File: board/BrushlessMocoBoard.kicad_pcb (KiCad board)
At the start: 4 copper layers, 107.6 x 86.6 mm, 117 parts, among them J1 Conn_01x03, J2 Conn_01x03, J3 Conn_01x03, SW1 SW_Push, SW2 SW_Push, U1 STSPIN32G4TR, U2 SN65HVD232

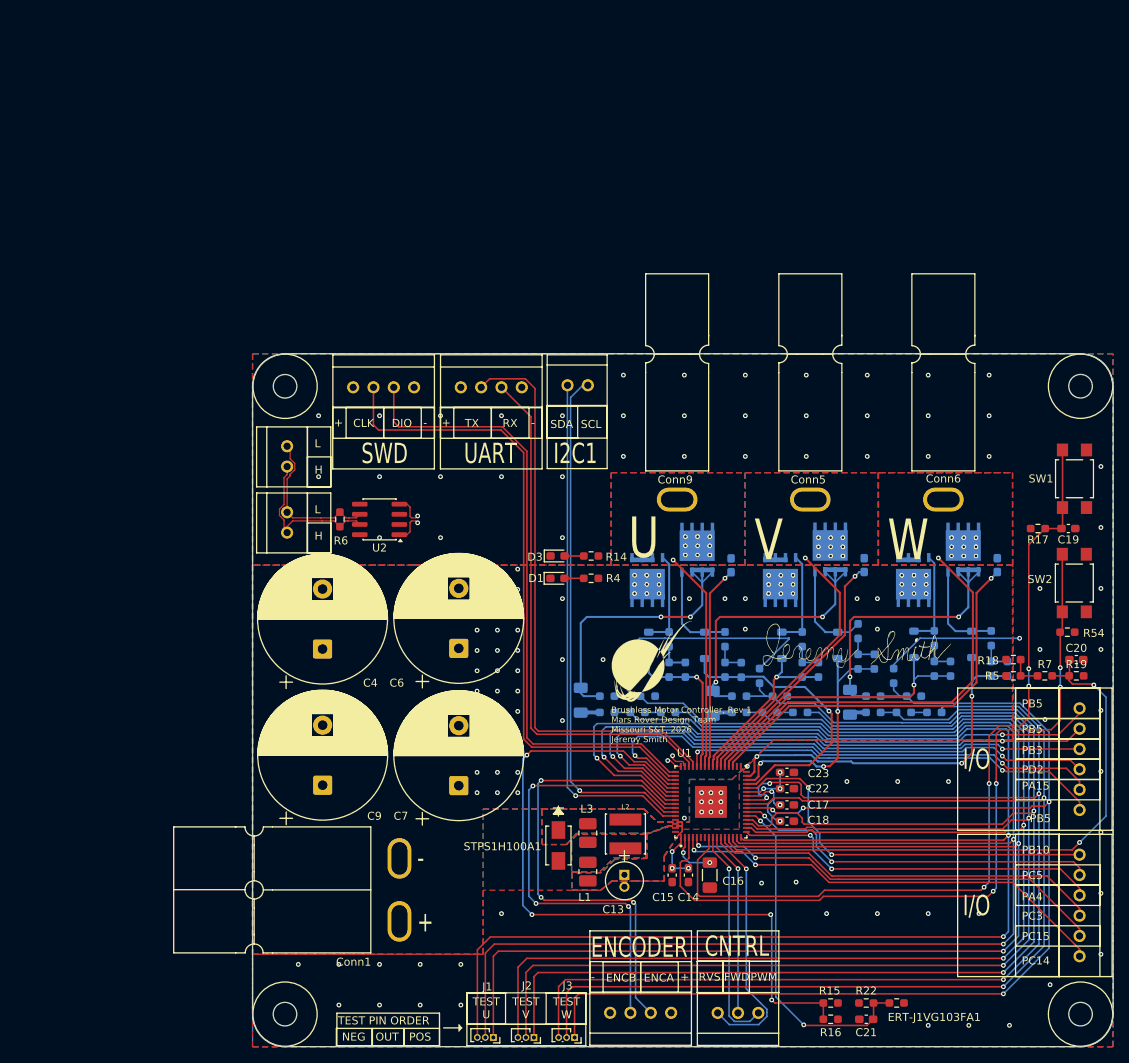
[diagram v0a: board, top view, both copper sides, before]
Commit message: Fixed many issues found in Rev1 review prior to order
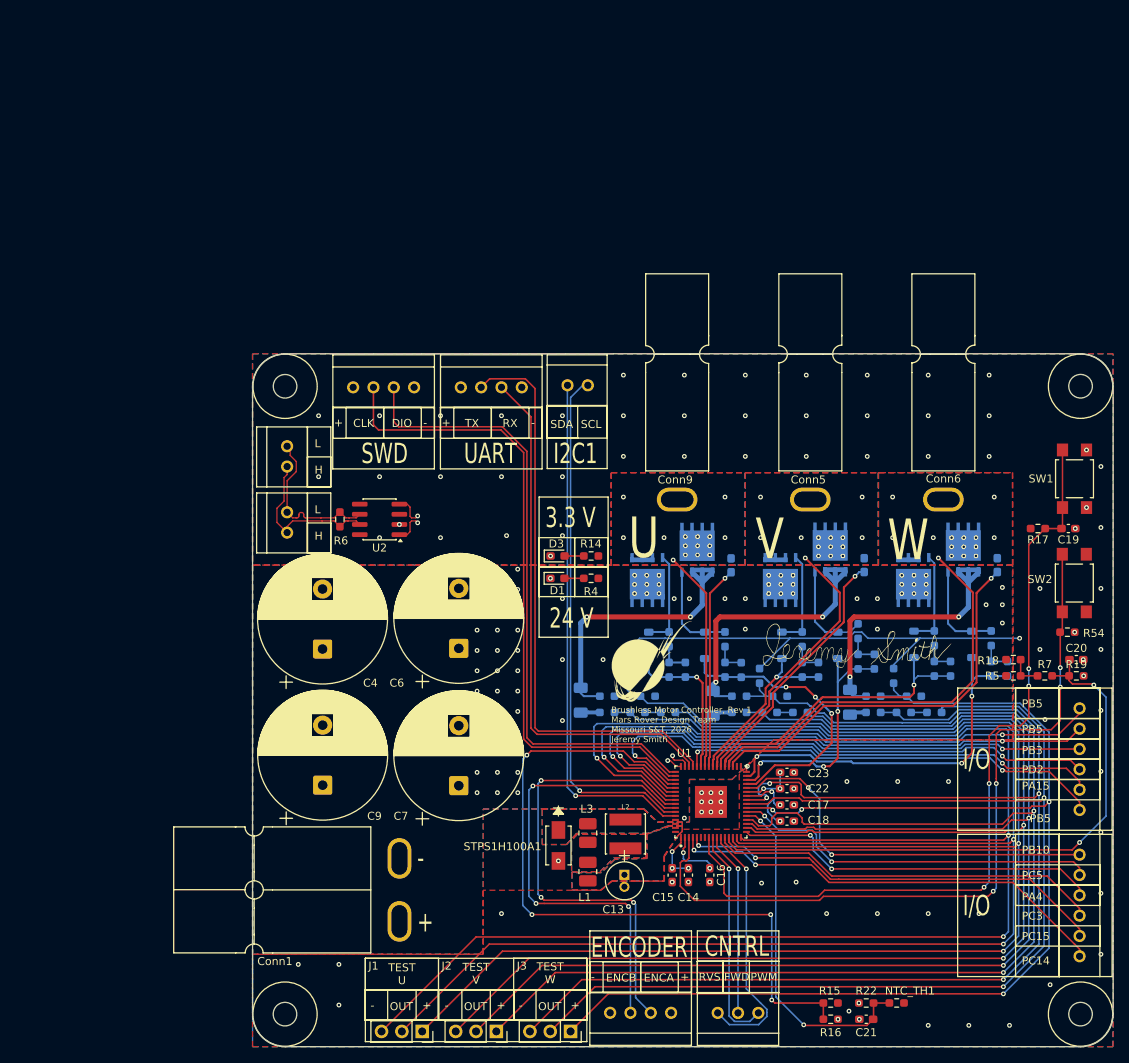
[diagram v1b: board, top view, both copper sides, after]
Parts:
- C13: value EEAGA1E100H -> 10 µF / 25 V
- C16: value 100 μF / 6.3 V -> 100 nF / 6.3 V; footprint Capacitor_SMD:C_1206_3216Metric_Pad1.33x1.80mm_HandSolder -> Capacitor_SMD:C_0603_1608Metric_Pad1.08x0.95mm_HandSolder
- J1, J2, J3: footprint Connector_PinSocket_1.00mm:PinSocket_1x03_P1.00mm_Vertical -> Connector_PinSocket_2.54mm:PinSocket_1x03_P2.54mm_Vertical
- R14: value 100 Ω -> 470 Ω
- R4: value 1.5 kΩ -> 6.8 kΩ
- moved J1 8.93 mm to (51.0, 125.2)
- moved J2 4.76 mm to (60.3, 125.2)
- moved J3 0.91 mm to (69.6, 125.2)
- renumbered ERT-J1VG103FA1 to NTC_TH1, MOSFET1 to Q1, MOSFET2 to Q2, MOSFET3 to Q3, MOSFET4 to Q4, MOSFET5 to Q5, MOSFET6 to Q6
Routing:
- net +3.3V: track 74.8 -> 92.7 mm, vias 81 -> 77
- net /Half-Bridges & Current Sensing/OPN_U: track 188.5 -> 193.8 mm
- net /Half-Bridges & Current Sensing/OPO_U: track 182.5 -> 186.4 mm
- net Net-(U1-PG10): track 105.6 -> 102.4 mm
- net /Half-Bridges & Current Sensing/OPP_W: track 157.4 -> 154.7 mm
- net /Half-Bridges & Current Sensing/OPP_U: track 194.4 -> 197.0 mm
- net /Half-Bridges & Current Sensing/OPN_V: track 171.6 -> 173.9 mm
- net /Half-Bridges & Current Sensing/OPO_W: track 147.0 -> 145.5 mm
- net /Half-Bridges & Current Sensing/OPO_V: track 164.7 -> 165.9 mm
- net CAN-: track 19.2 -> 20.2 mm
- net GND: track 1.54 -> 2.29 mm, vias 10 -> 30
- net /Half-Bridges & Current Sensing/GLS_U: vias 1 -> 3
- net /Half-Bridges & Current Sensing/OUT_W: vias 10 -> 15
- net /Half-Bridges & Current Sensing/OUT_V: vias 10 -> 15
- net 24 V: vias 76 -> 80
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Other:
- board text added: "24 V"
- board text added: "3.3 V"
- board text removed: "NEG"
- board text removed: "POS"
- board text removed: "TEST PIN ORDER"

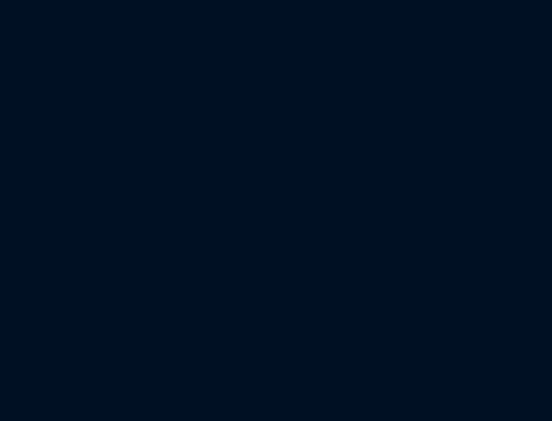
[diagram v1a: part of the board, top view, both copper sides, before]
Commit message: Added Cvm to schematic, need to add to layout as well
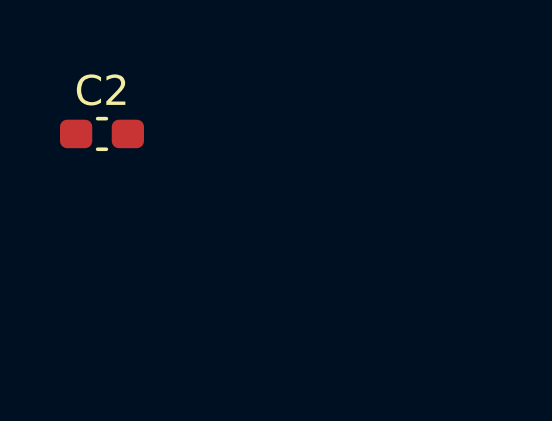
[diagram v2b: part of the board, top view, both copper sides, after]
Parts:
- added C2: 220 nF / 100 V, Capacitor_SMD:C_0603_1608Metric_Pad1.08x0.95mm_HandSolder, F.Cu at (1.68, 0.76)
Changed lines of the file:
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@@
+		)
+	)
+	(footprint "Capacitor_SMD:C_0603_1608Metric_Pad1.08x0.95mm_HandSolder"
+		(layer "F.Cu")
+		(at 1.675 0.755)
+		(descr "Capacitor SMD 0603 (1608 Metric), square (rectangular) end terminal, IPC-7351 nominal with elongated pad for handsoldering. (Body size source: IPC-SM-782 page 76, https://www.pcb-3d.com/wordpress/wp-content/uploads/ipc-sm-782a_amendment_1_and_2.pdf), generated with kicad-footprint-generator")
+		(tags "capacitor handsolder")
+		(property "Reference" "C2"
+			(at 0 -1.43 0)
+			(layer "F.SilkS")
+			(effects
+				(font
+					(size 1 1)
+					(thickness 0.15)
+				)
+			)
+		)
+		(property "Value" "220 nF / 100 V"
+			(at 0 1.43 0)
+			(layer "F.Fab")
+			(effects
+				(font
+					(size 1 1)
+					(thickness 0.15)
+				)
+			)
+		)
+		(property "Datasheet" "~"
+			(at 0 0 0)
+			(layer "F.Fab")
+			(hide yes)
+			(effects
+				(font
+					(size 1.27 1.27)
+					(thickness 0.15)
+				)
+			)
+		)
+		(property "Description" "Unpolarized capacitor"
+			(at 0 0 0)
+			(layer "F.Fab")
+			(hide yes)
+			(effects
+				(font
+					(size 1.27 1.27)
+					(thickness 0.15)
+				)
+			)
+		)
+		(property ki_fp_filters "C_*")
+		(sheetname "/MCU/")
+		(sheetfile "MCU.kicad_sch")
+		(attr smd)
+		(fp_line
+			(start -0.146267 -0.51)
+			(end 0.146267 -0.51)
+			(stroke
+				(width 0.12)
+				(type solid)
+			)
+			(layer "F.SilkS")
+		)
+		(fp_line
+			(start -0.146267 0.51)
+			(end 0.146267 0.51)
+			(stroke
+				(width 0.12)
+				(type solid)
+			)
+			(layer "F.SilkS")
+		)
+		(fp_line
+			(start -1.65 -0.73)
+			(end 1.65 -0.73)
+			(stroke
+				(width 0.05)
+				(type solid)
+			)
+			(layer "F.CrtYd")
+		)
+		(fp_line
+			(start -1.65 0.73)
+			(end -1.65 -0.73)
+			(stroke
+				(width 0.05)
+				(type solid)
+			)
+			(layer "F.CrtYd")
+		)
+		(fp_line
+			(start 1.65 -0.73)
+			(end 1.65 0.73)
+			(stroke
+				(width 0.05)
+				(type solid)
+			)
+			(layer "F.CrtYd")
+		)
+		(fp_line
+			(start 1.65 0.73)
+			(end -1.65 0.73)
+			(stroke
+				(width 0.05)
+				(type solid)
+			)
+			(layer "F.CrtYd")
+		)
+		(fp_line
+			(start -0.8 -0.4)
+			(end 0.8 -0.4)
+			(stroke
+				(width 0.1)
+				(type solid)
+			)
+			(layer "F.Fab")
+		)
+		(fp_line
+			(start -0.8 0.4)
+			(end -0.8 -0.4)
+			(stroke
+				(width 0.1)
+				(type solid)
+			)
+			(layer "F.Fab")
+		)
+		(fp_line
+			(start 0.8 -0.4)
+			(end 0.8 0.4)
+			(stroke
+				(width 0.1)
+				(type solid)
+			)
+			(layer "F.Fab")
+		)
+		(fp_line
+			(start 0.8 0.4)
+			(end -0.8 0.4)
+			(stroke
+				(width 0.1)
+				(type solid)
+			)
+			(layer "F.Fab")
+		)
+		(fp_text user "${REFERENCE}"
+			(at 0 0 0)
+			(layer "F.Fab")
+			(effects
+				(font
+					(size 0.4 0.4)
+					(thickness 0.06)
+				)
+			)
+		)
+		(pad "1" smd roundrect
+			(at -0.8625 0)
+			(size 1.075 0.95)
+			(layers "F.Cu" "F.Mask" "F.Paste")
+			(roundrect_rratio 0.25)
+			(net 4 "24 V")
+			(pintype "passive")
+		)
+		(pad "2" smd roundrect
+			(at 0.8625 0)
+			(size 1.075 0.95)
+			(layers "F.Cu" "F.Mask" "F.Paste")
+			(roundrect_rratio 0.25)
+			(net 77 "GND")
+			(pintype "passive")
+		)
+		(embedded_fonts no)
+		(model "${KICAD9_3DMODEL_DIR}/Capacitor_SMD.3dshapes/C_0603_1608Metric.step"
+			(offset
+				(xyz 0 0 0)
+			)
+			(scale
+				(xyz 1 1 1)
+			)
+			(rotate
+				(xyz 0 0 0)
+			)
 		)
 	)

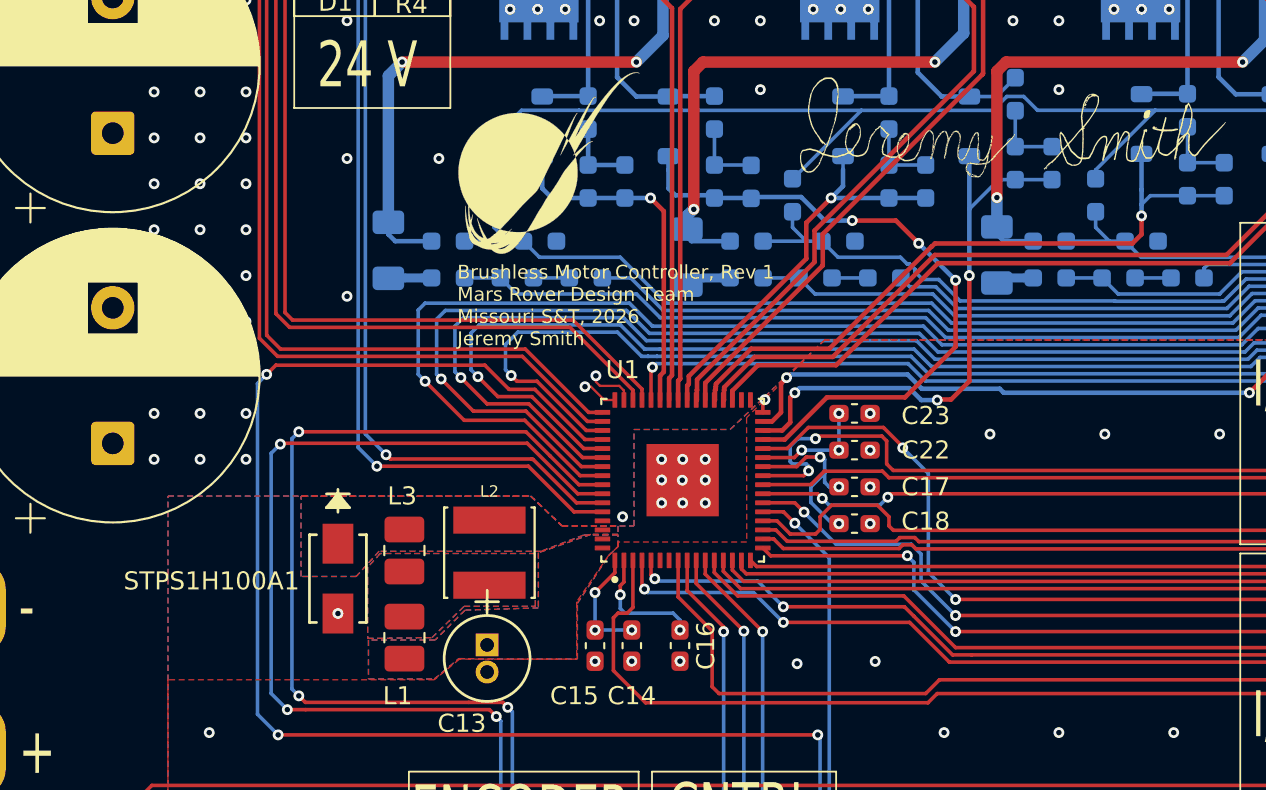
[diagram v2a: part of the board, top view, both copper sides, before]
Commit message: Added footprints to board library
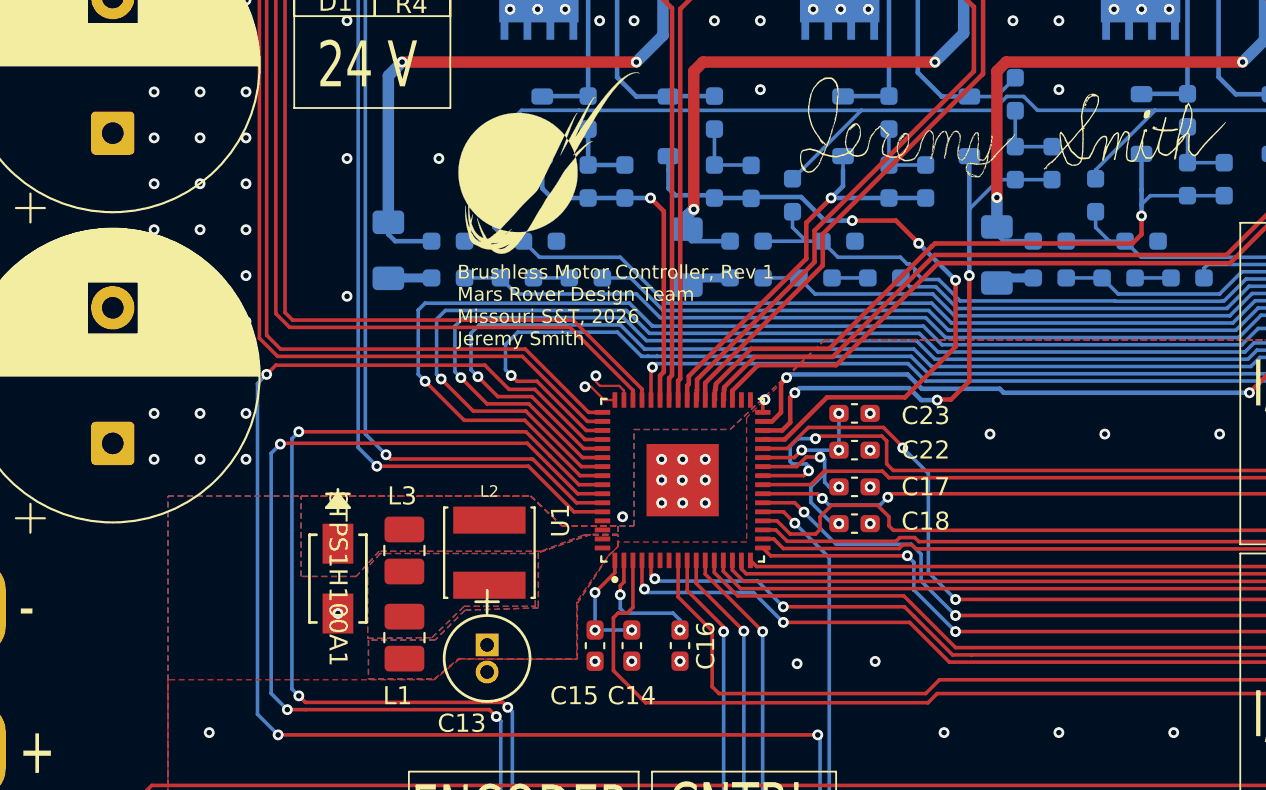
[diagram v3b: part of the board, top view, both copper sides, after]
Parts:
- Q1, Q2, Q3, Q4, Q5, Q6: footprint BoCoFootprintLibrary:PG-TDSON-8_INF -> BrushlessMocoBoard:PG-TDSON-8_INF
- STPS1H100A1: footprint BoCoFootprintLibrary:SMA_STM -> BrushlessMocoBoard:SMA_STM
- U1: footprint STSPIN32G4TR:QFN50P900X900X100-65N -> BrushlessMocoBoard:QFN50P900X900X100-65N
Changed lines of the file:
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@@
 		(embedded_fonts no)
 	)
-	(footprint "STSPIN32G4TR:QFN50P900X900X100-65N"
+	(footprint "BrushlessMocoBoard:QFN50P900X900X100-65N"
 		(layer "F.Cu")
 		(at 87.142 96.53 90)
 		(property "Reference" "U1"
-			(at 6.106 -3.322 180)
+			(at -2.235 -6.75 90)
 			(layer "F.SilkS")
 			(effects
@@
 		)
 		(property "Value" "STSPIN32G4TR"
-			(at 0 0 180)
+			(at 7.925 6.75 90)
 			(layer "F.Fab")
 			(effects
@@
 		)
 	)
-	(footprint "BoCoFootprintLibrary:SMA_STM"
+	(footprint "BrushlessMocoBoard:SMA_STM"
 		(layer "F.Cu")
 		(at 68.077242 101.973356 -90)
 		(tags "STPS1H100A ")
 		(property "Reference" "STPS1H100A1"
-			(at 0.134644 6.990242 0)
+			(at 0 0 270)
 			(unlocked yes)
 			(layer "F.SilkS")
@@
 		)
 		(property "Datasheet" "https://www.st.com/resource/en/datasheet/stps1h100.pdf"
-			(at 0 0 90)
+			(at 0 0 270)
 			(layer "F.Fab")
 			(hide yes)
@@
 		)
 		(property "Description" ""
-			(at 0 0 90)
+			(at 0 0 270)
 			(layer "F.Fab")
 			(hide yes)
@@
 			(pintype "unspecified")
 		)
+		(zone
+			(net 0)
+			(net_name "")
+			(layer "F.Cu")
+			(hatch full 0.508)
+			(connect_pads
+				(clearance 0)
+			)
+			(min_thickness 0.254)
+			(filled_areas_thickness no)
+			(keepout
+				(tracks not_allowed)
+				(vias not_allowed)
+				(pads allowed)
+				(copperpour not_allowed)
+				(footprints allowed)
+			)
+			(placement
+				(enabled no)
+				(sheetname "")
+			)
+			(fill
+				(thermal_gap 0.508)
+				(thermal_bridge_width 0.508)
+			)
+			(polygon
+				(pts
+					(xy 69.474242 101.198656) (xy 69.474242 102.748056) (xy 66.680242 102.748056) (xy 66.680242 101.198656)
+				)
+			)
+		)
 		(embedded_fonts no)
 	)
@@
 		)
 	)
-	(footprint "BoCoFootprintLibrary:PG-TDSON-8_INF"
+	(footprint "BrushlessMocoBoard:PG-TDSON-8_INF"
 		(layer "B.Cu")
 		(at 112.465201 68.797496 -90)
 		(tags "BSC035N10NS5ATMA1 ")
 		(property "Reference" "Q5"
-			(at -4.535496 0.324201 0)
+			(at 0 0 90)
 			(unlocked yes)
 			(layer "B.SilkS")
@@
 		)
 	)
-	(footprint "BoCoFootprintLibrary:PG-TDSON-8_INF"
+	(footprint "BrushlessMocoBoard:PG-TDSON-8_INF"
 		(layer "B.Cu")
 		(at 118.688201 64.987496 90)
 		(tags "BSC035N10NS5ATMA1 ")
 		(property "Reference" "Q6"
-			(at -4.735504 0.437799 0)
+			(at 0 0 270)
 			(unlocked yes)
 			(layer "B.SilkS")
@@
 		)
 	)
-	(footprint "BoCoFootprintLibrary:PG-TDSON-8_INF"
+	(footprint "BrushlessMocoBoard:PG-TDSON-8_INF"
 		(layer "B.Cu")
 		(at 95.828201 68.797496 -90)
 		(tags "BSC035N10NS5ATMA1 ")
 		(property "Reference" "Q3"
-			(at -4.535496 0.197201 0)
+			(at 0 0 90)
 			(unlocked yes)
 			(layer "B.SilkS")
@@
 		)
 	)
-	(footprint "BoCoFootprintLibrary:PG-TDSON-8_INF"
+	(footprint "BrushlessMocoBoard:PG-TDSON-8_INF"
 		(layer "B.Cu")
 		(at 85.4202 65.0113 90)
 		(tags "BSC035N10NS5ATMA1 ")
 		(property "Reference" "Q2"
-			(at -4.8387 0.0508 0)
+			(at 0 0 270)
 			(unlocked yes)
 			(layer "B.SilkS")
@@
 		)
 	)
-	(footprint "BoCoFootprintLibrary:PG-TDSON-8_INF"
+	(footprint "BrushlessMocoBoard:PG-TDSON-8_INF"
 		(layer "B.Cu")
 		(at 102.051201 64.974796 90)
 		(tags "BSC035N10NS5ATMA1 ")
 		(property "Reference" "Q4"
-			(at -4.748204 0.183799 0)
+			(at 0 0 270)
 			(unlocked yes)
 			(layer "B.SilkS")
@@
 		)
 	)
-	(footprint "BoCoFootprintLibrary:PG-TDSON-8_INF"
+	(footprint "BrushlessMocoBoard:PG-TDSON-8_INF"
 		(layer "B.Cu")
 		(at 79.191201 68.797496 -90)
 		(tags "BSC035N10NS5ATMA1 ")
 		(property "Reference" "Q1"
-			(at -4.535496 0.197201 0)
+			(at 0 0 90)
 			(unlocked yes)
 			(layer "B.SilkS")
@@
 		(width 0.2)
 		(layer "B.Cu")
-		(net 9)
-	)
-	(segment
-		(start 113.281 76.073)
-		(end 113.278 76.076)
-		(width 0.2)
-		(layer "B.Cu")

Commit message: Final board as ordered
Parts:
- moved C2 121.7 mm to (76.7, 96.5), turned to 180 degrees
- moved R54 4.15 mm to (129.0, 72.1), turned to -90 degrees
- moved C20 0.51 mm to (132.8, 79.2)
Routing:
- net 24 V: track 0.00 -> 6.07 mm
- net Net-(U1-PC13): track 96.6 -> 98.7 mm
- net GND: track 2.29 -> 3.46 mm, vias 30 -> 31
- net Net-(U1-PA0): track 75.0 -> 74.5 mm

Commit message: Fixed i/o pin silkscreen labels
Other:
- board text added: "PA8"
- board text added: "PB4"
